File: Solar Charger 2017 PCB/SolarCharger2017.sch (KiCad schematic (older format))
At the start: 21 parts, among them P1 5V OUT, P2 LiIon Cell V, P3 PV IN 1, P4 PV IN 2, SW1 SPST, U1 BQ24210

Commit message: Update of PCB
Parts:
- added P5: LiIon Cell V, REInnovationFootprint:SIL_2_screw_+_JST_2mm, symbol CONN_01X02
- added P6: 5V OUT, REInnovationFootprint:SIL-2_screw_terminal, symbol CONN_01X02
- BT1: value LiIon Cell -> 18650 LiIon Cell
- DCDC1, DCDC2: value DC-DC_GENERIC -> DC-DC
- P3, P4: footprint REInnovationFootprint:SIL-2_screw_terminal -> REInnovationFootprint:SIL_2_screw_+_JST_2mm
- PCB1: footprint REInnovationFootprint:PCB_65x65mm -> REInnovationFootprint:PCB_65x90mm
- SC1: footprint REInnovationFootprint:PV_130mmx65mm -> REInnovationFootprint:PV_130mmx65mm_NoOutline
- SW1: value SPST -> 5V ON
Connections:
- net GND: now also P5.2 (P2)
- net VCC: now also P5.1 (P1)
- net at DCDC1.3 (+Vout), DCDC2.3 (+Vout), P1.1 (P1): now also P6.1 (P1)
- net at DCDC1.4 (-Vout), DCDC2.4 (-Vout), P1.2 (P2): now also P6.2 (P2)
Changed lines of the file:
@@
 P 7050 2950
 F 0 "BT1" H 7150 3050 50  0000 L CNN
-F 1 "LiIon Cell" H 7150 2950 50  0000 L CNN
+F 1 "18650 LiIon Cell" H 7150 2950 50  0000 L CNN
 F 2 "REInnovationFootprint:TH_LiIon_Holder" V 7050 3010 50  0001 C CNN
 F 3 "" V 7050 3010 50  0000 C CNN
@@
 F 0 "SC1" H 2100 2900 50  0000 L CNN
 F 1 "PV <2W 5.5V" H 2100 2800 50  0000 L CNN
-F 2 "REInnovationFootprint:PV_130mmx65mm" V 2000 2860 50  0001 C CNN
+F 2 "REInnovationFootprint:PV_130mmx65mm_NoOutline" V 2000 2860 50  0001 C CNN
 F 3 "" V 2000 2860 50  0000 C CNN
 	1    2000 2800
@@
 P 8800 4700
 F 0 "DCDC1" H 8600 4900 50  0000 C CNN
-F 1 "DC-DC_GENERIC" H 9000 4350 50  0000 C CNN
+F 1 "DC-DC" H 9000 4350 50  0000 C CNN
 F 2 "REInnovationFootprint:TH_DCDC_Converter_USB" H 8800 4700 60  0001 C CNN
 F 3 "" H 8800 4700 60  0000 C CNN
@@
 P 7550 4650
 F 0 "SW1" H 7550 4750 50  0000 C CNN
-F 1 "SPST" H 7550 4550 50  0000 C CNN
+F 1 "5V ON" H 7550 4550 50  0000 C CNN
 F 2 "matts_components:SW_SPDT_rapid_760271" H 7550 4650 50  0001 C CNN
 F 3 "" H 7550 4650 50  0000 C CNN
@@
 F 0 "P3" H 2800 1950 50  0000 C CNN
 F 1 "PV IN 1" V 2900 1800 50  0000 C CNN
-F 2 "REInnovationFootprint:SIL-2_screw_terminal" H 2800 1800 50  0001 C CNN
+F 2 "REInnovationFootprint:SIL_2_screw_+_JST_2mm" H 2800 1800 50  0001 C CNN
 F 3 "" H 2800 1800 50  0000 C CNN
 	1    2800 1800
@@
 F 0 "P4" H 3400 1950 50  0000 C CNN
 F 1 "PV IN 2" V 3500 1800 50  0000 C CNN
-F 2 "REInnovationFootprint:SIL-2_screw_terminal" H 3400 1800 50  0001 C CNN
+F 2 "REInnovationFootprint:SIL_2_screw_+_JST_2mm" H 3400 1800 50  0001 C CNN
 F 3 "" H 3400 1800 50  0000 C CNN
 	1    3400 1800
@@
 F 0 "PCB1" H 10000 3400 50  0000 C CNN
 F 1 "PCB" V 10100 3300 50  0000 C CNN
-F 2 "REInnovationFootprint:PCB_65x65mm" H 10000 3300 50  0001 C CNN
+F 2 "REInnovationFootprint:PCB_65x90mm" H 10000 3300 50  0001 C CNN
 F 3 "" H 10000 3300 50  0000 C CNN
 	1    10000 3300
@@
 P 8800 5600
 F 0 "DCDC2" H 8600 5800 50  0000 C CNN
-F 1 "DC-DC_GENERIC" H 9000 5250 50  0000 C CNN
+F 1 "DC-DC" H 9000 5250 50  0000 C CNN
 F 2 "REInnovationFootprint:TH_DCDC_Converter_NoUSB" H 8800 5600 60  0001 C CNN
 F 3 "" H 8800 5600 60  0000 C CNN
@@
 	8050 5800 8200 5800
 Connection ~ 8050 4900
+$Comp
+L CONN_01X02 P6
+U 1 1 593EA27A
+P 9800 5200
+F 0 "P6" H 9800 5350 50  0000 C CNN
+F 1 "5V OUT" V 9900 5200 50  0000 C CNN
+F 2 "REInnovationFootprint:SIL-2_screw_terminal" H 9800 5200 50  0001 C CNN
+F 3 "" H 9800 5200 50  0000 C CNN
+	1    9800 5200
+	1    0    0    -1
+$EndComp
+$Comp
+L CONN_01X02 P5
+U 1 1 593EA2E6
+P 8950 3450
+F 0 "P5" H 8950 3600 50  0000 C CNN
+F 1 "LiIon Cell V" V 9050 3450 50  0000 C CNN
+F 2 "REInnovationFootprint:SIL_2_screw_+_JST_2mm" H 8950 3450 50  0001 C CNN
+F 3 "" H 8950 3450 50  0000 C CNN
+	1    8950 3450
+	1    0    0    -1
+$EndComp
+Wire Wire Line
+	8750 3400 8700 3400
+Wire Wire Line
+	8700 3400 8700 2850
+Connection ~ 8700 2850
+Wire Wire Line
+	8750 3500 8650 3500
+Wire Wire Line
+	8650 3500 8650 2950
+Connection ~ 8650 2950
+Wire Wire Line
+	9600 5150 9500 5150
+Connection ~ 9500 5150
+Wire Wire Line
+	9600 5250 9550 5250
+Connection ~ 9550 5250
 $EndSCHEMATC

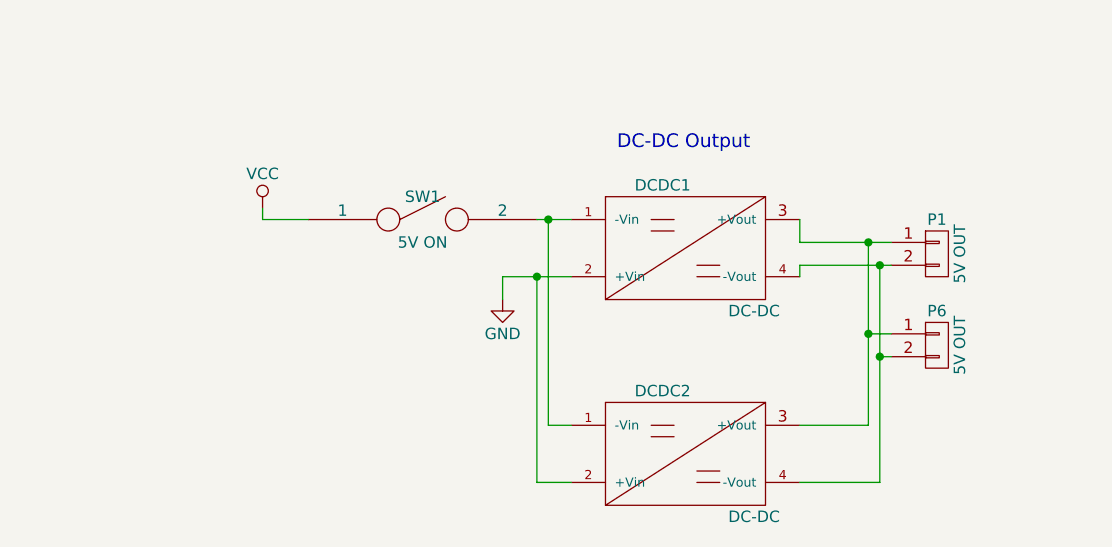
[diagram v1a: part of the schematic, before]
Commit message: Changes to PCB
DC-DC converter correct. Moved silkscreen. Sorted costs
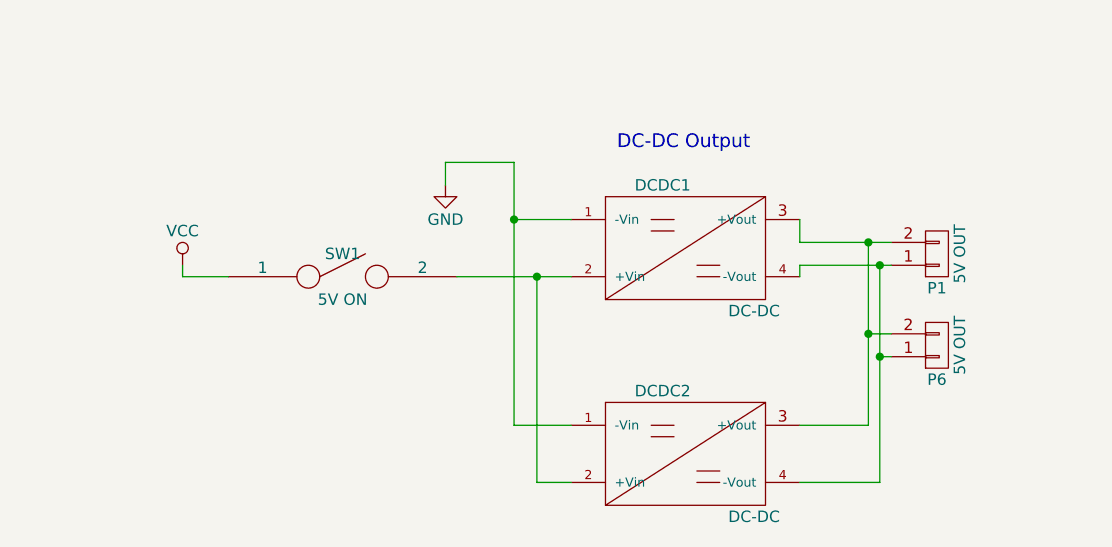
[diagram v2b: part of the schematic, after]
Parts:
- BT1: Description (none) -> 18650 PCB mount holder; Supplier 1 (none) -> eBay; Supplier 1 Cost (none) -> 0.50; Supplier 1 Part No (none) -> http://www.ebay.co.uk/itm/122466718109
- C1: Supplier 1 Cost (none) -> 0.1
- C2: Supplier 1 Cost (none) -> 0.10
- D2, D3: Supplier 1 Cost (none) -> 0.05
- DCDC1: Supplier 1 (none) -> Aliexpress; Supplier 1 Cost (none) -> 1.5
- DCDC2: Supplier 1 (none) -> Aliexpress; Supplier 1 Cost (none) -> 1
- R1, R2, R3, R4: Supplier 1 Cost (none) -> 0.01
- SC1: Description (none) -> 1-2W solar PV module; Supplier 1 (none) -> Aliexpress; Supplier 1 Cost (none) -> 2.5
- SW1: footprint matts_components:SW_SPDT_rapid_760271 -> REInnovationFootprint:SW_SPDT_R_Angle_ALIEX; Supplier 1 (none) -> Aliexpress; Supplier 1 Cost (none) -> 0.2
- U1: Manufacturer (none) -> Texas Instruments; Manufacturer Part No (none) -> BQ24210; Supplier 1 (none) -> RS; Supplier 1 Cost (none) -> 2.88; Supplier 1 Part No (none) -> 742-2836
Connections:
- net GND: now also DCDC1.1 (-Vin), DCDC2.1 (-Vin); no longer DCDC1.2 (+Vin), DCDC2.2 (+Vin)
- net at DCDC1.3 (+Vout), DCDC2.3 (+Vout): now also P1.2 (P2), P6.2 (P2); no longer P1.1 (P1), P6.1 (P1)
- net at DCDC1.4 (-Vout), DCDC2.4 (-Vout): now also P1.1 (P1), P6.1 (P1); no longer P1.2 (P2), P6.2 (P2)
- new net: DCDC1.2 (+Vin), DCDC2.2 (+Vin), SW1.2
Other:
- moved on the sheet: SW1
